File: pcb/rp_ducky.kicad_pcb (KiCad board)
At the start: 4 copper layers, 14 x 30 mm, 34 parts, among them J1 USB_A, Q1 2N7002, SW1 R-667799, SW2 R-667799, U1 TCR2EE33, U2 W25Q32JVZP, U3 RP2040, U4 D1213A-04V, Y1 Crystal_GND24

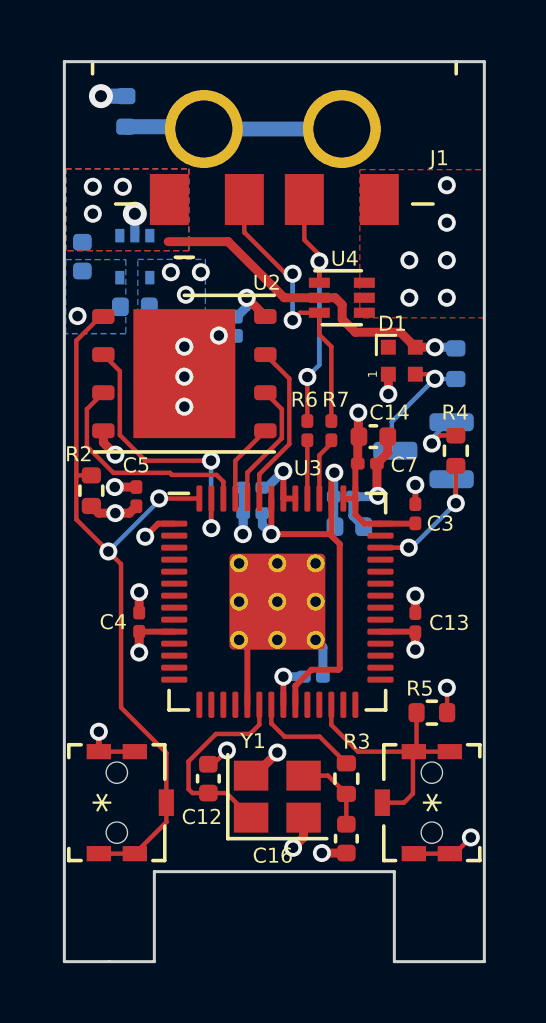
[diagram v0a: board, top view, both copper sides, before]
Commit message: remove level shifter for the SK8012 rgb led
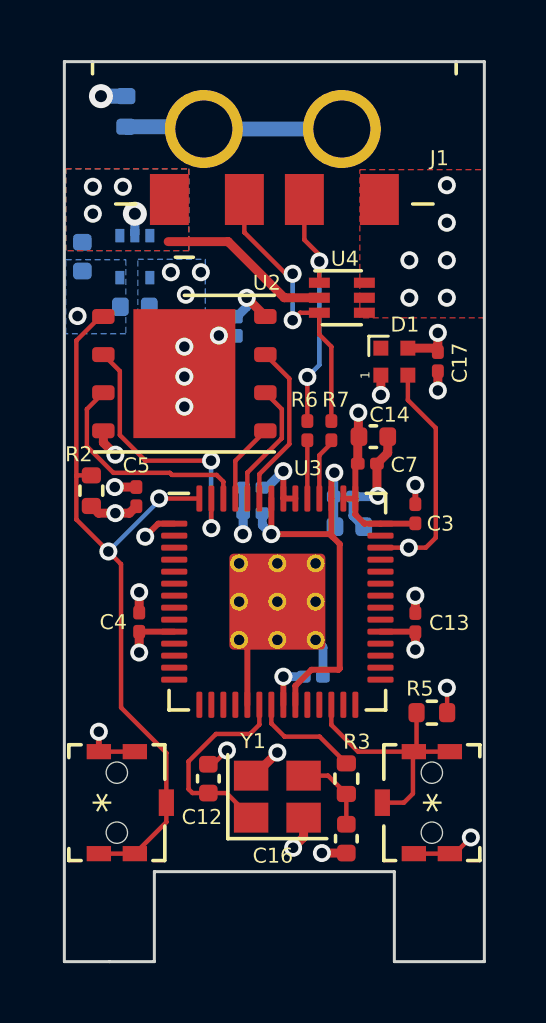
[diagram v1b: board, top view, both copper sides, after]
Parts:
- removed Q1: 2N7002, Package_TO_SOT_SMD:SOT-23
- removed R4, R8: 10k, Resistor_SMD:R_0402_1005Metric
- added C17: 0.1uF, Capacitor_SMD:C_0201_0603Metric, F.Cu at (92.5, 50.0)
- moved D1 0.25 mm to (91.0, 50.0)
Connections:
- D1 pad 2: /RGB_DI_5V -> /RGB_DI
- D1 pad 3: +5V -> +3V3
- U3 pad 40: /RGB_DI_3V3 -> /RGB_DI
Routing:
- net /RGB_DI: track 0.00 -> 7.78 mm, vias 0 -> 1
- net +5V: track 11.2 -> 5.81 mm, vias 4 -> 3
- net /RGB_DI_3V3: track 5.22 -> 0.00 mm, vias 2 -> 0
- net /RGB_DI_5V: track 4.40 -> 0.00 mm, vias 1 -> 0
- net GND: track 25.2 -> 25.8 mm, vias 27 -> 28
